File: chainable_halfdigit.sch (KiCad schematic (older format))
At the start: 48 parts, among them J1 Conn_01x03, J2 Conn_01x03

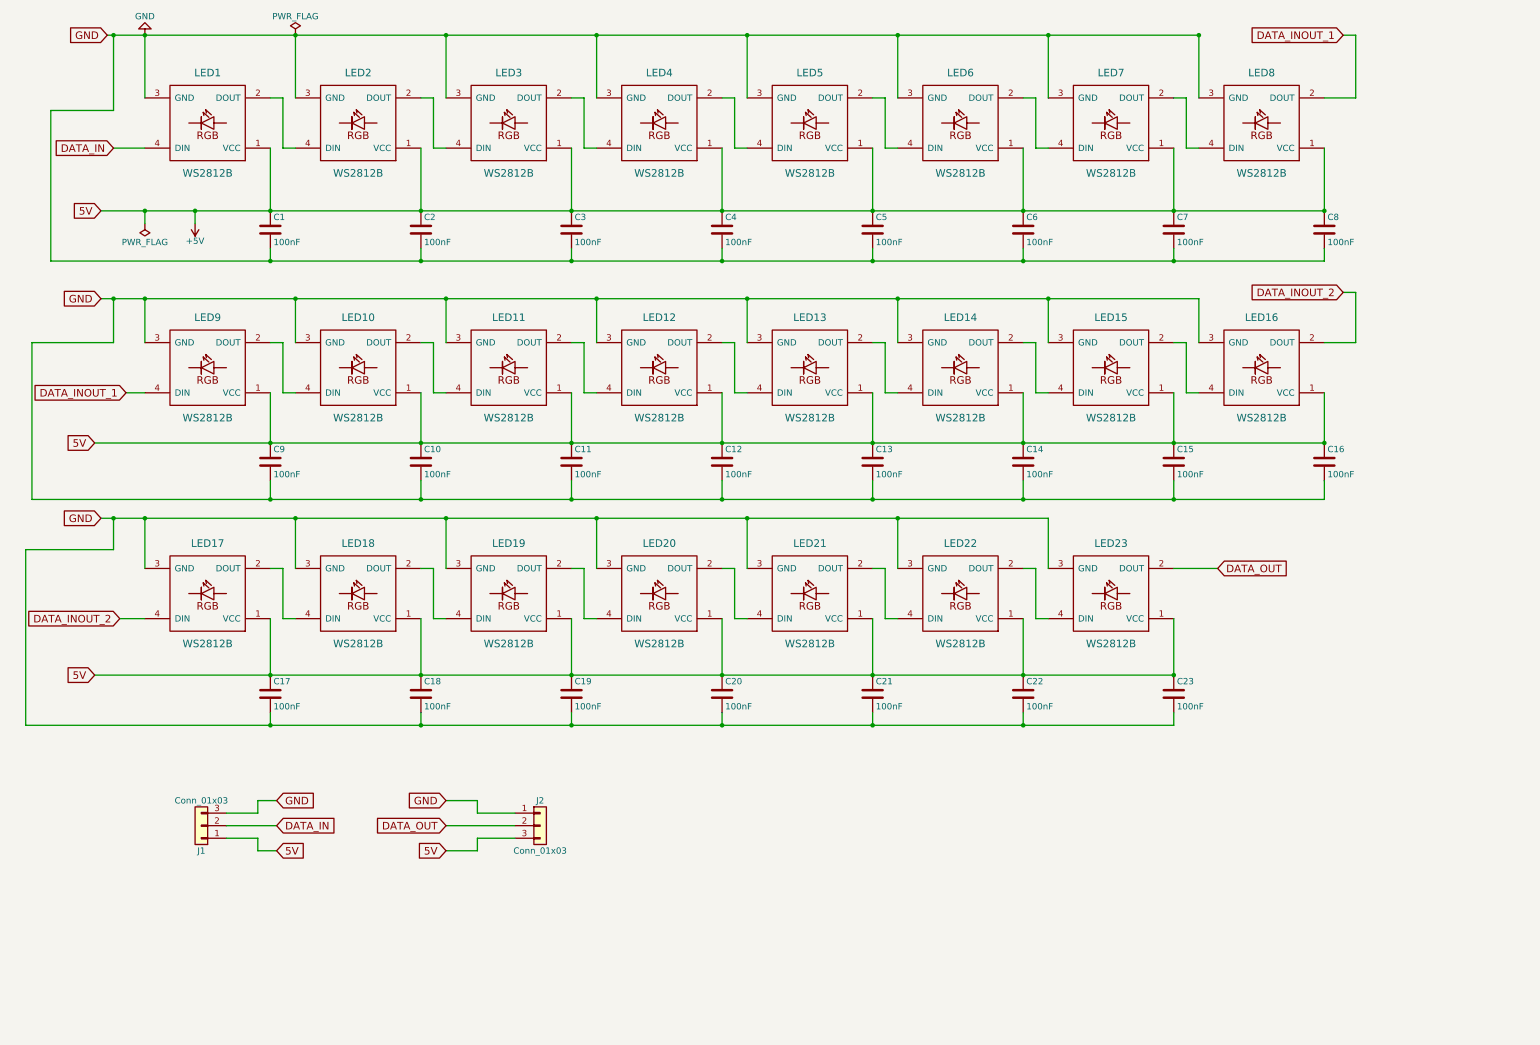
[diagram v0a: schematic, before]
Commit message: Added optionnal capacitors between 5v and gnd to make the pcb reversable
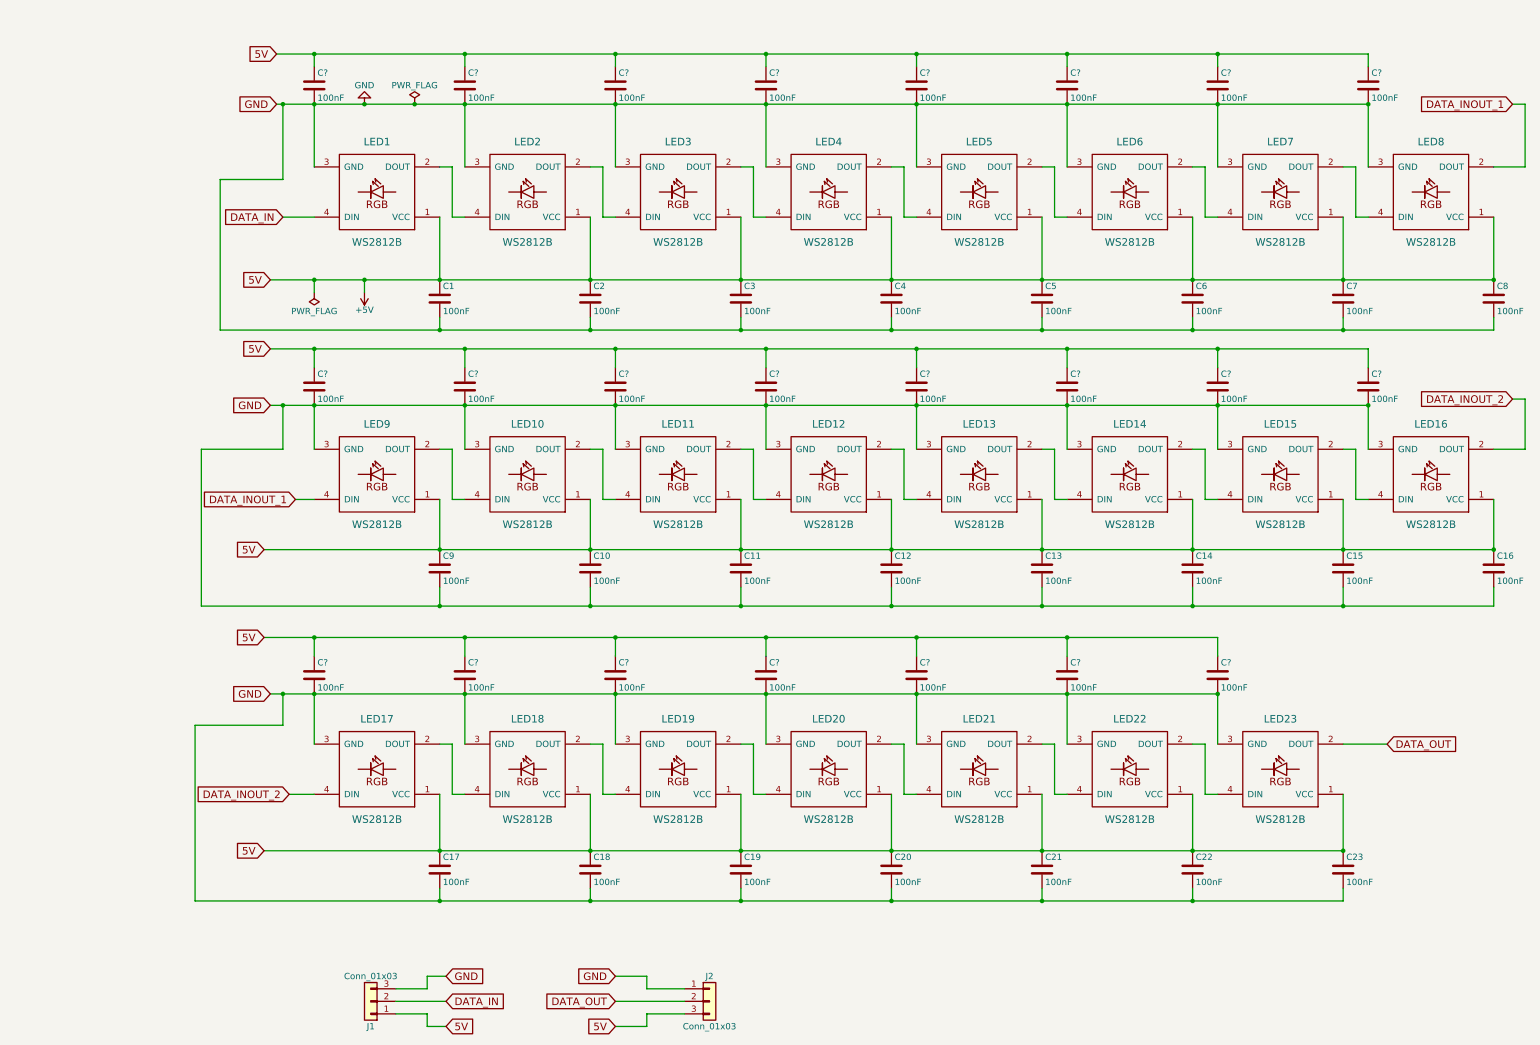
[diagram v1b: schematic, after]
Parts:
- added C? (x23): 100nF, Capacitors_SMD:C_0603, symbol C
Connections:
- net +5V: now also C?.1, C?.1, C?.1, C?.1, C?.1, C?.1, C?.1, C?.1, C?.1, C?.1, C?.1, C?.1, C?.1, C?.1, C?.1, C?.1, C?.1, C?.1, C?.1, C?.1, C?.1, C?.1, C?.1
- net GND: now also C?.2, C?.2, C?.2, C?.2, C?.2, C?.2, C?.2, C?.2, C?.2, C?.2, C?.2, C?.2, C?.2, C?.2, C?.2, C?.2, C?.2, C?.2, C?.2, C?.2, C?.2, C?.2, C?.2
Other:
- moved on the sheet: C1, C10, C11, C12, C13, C14, C15, C16, C17, C18, C19, C2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

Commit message: Revert "Added optionnal capacitors between 5v and gnd to make the pcb reversable"
This reverts commit ca0c5a413a5eb6350914f70d9c814ea12825b423.
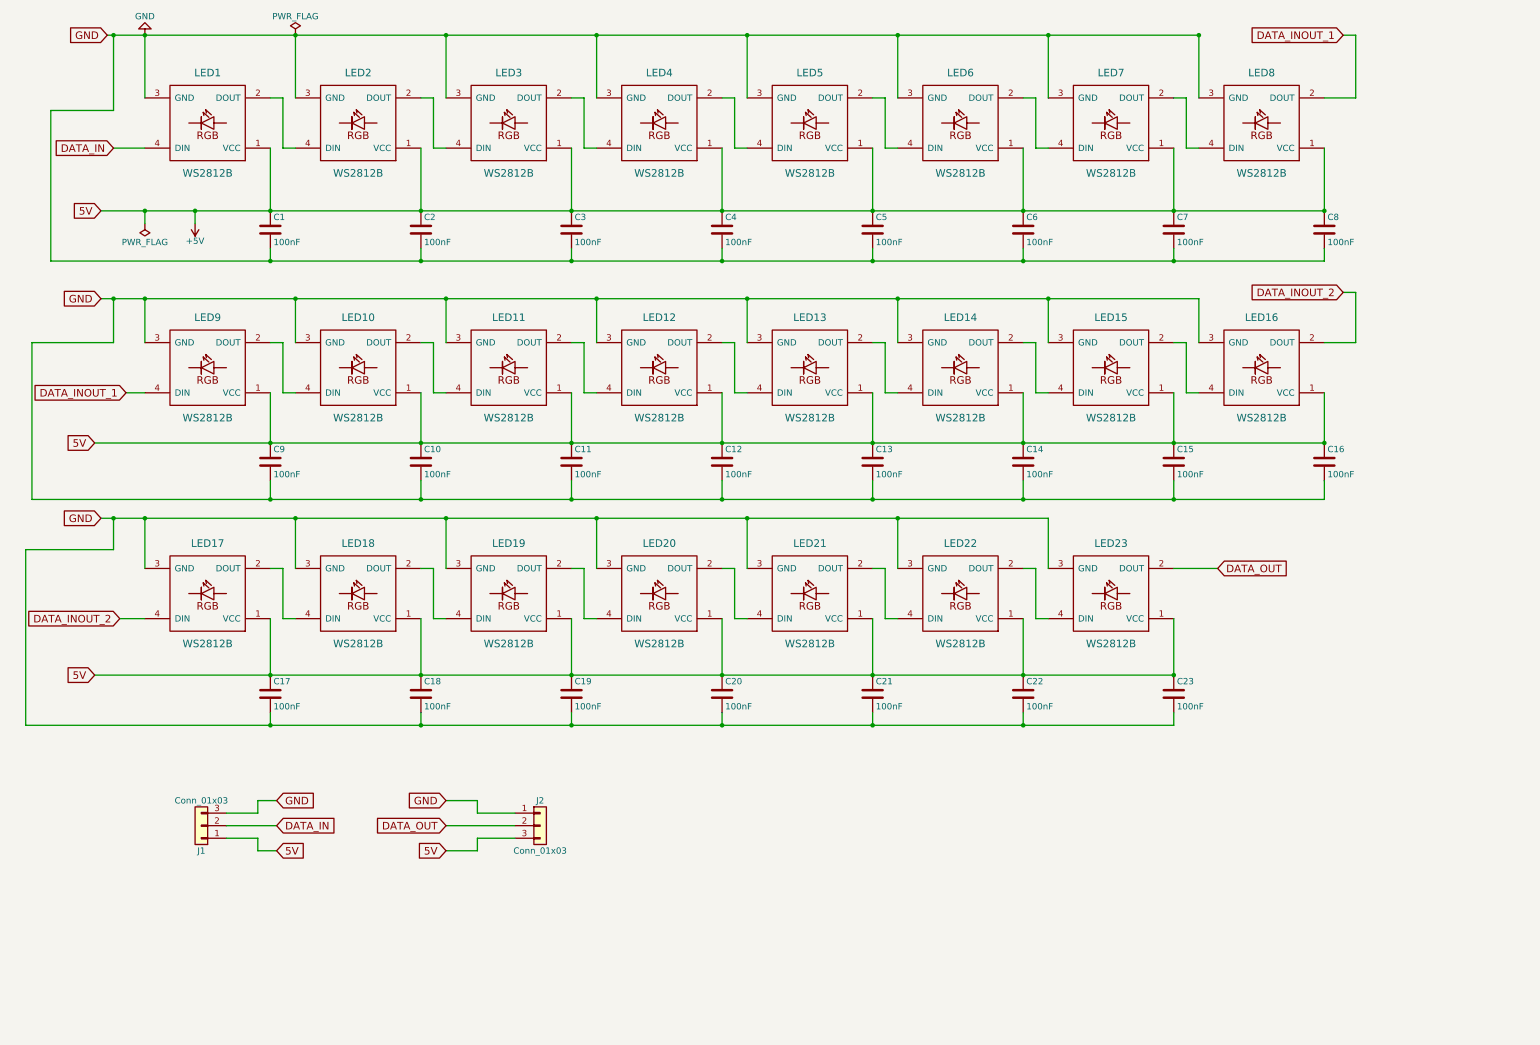
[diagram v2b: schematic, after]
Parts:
- removed C? (x23): 100nF, Capacitors_SMD:C_0603, symbol C
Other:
- moved on the sheet: C1, C10, C11, C12, C13, C14, C15, C16, C17, C18, C19, C2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
